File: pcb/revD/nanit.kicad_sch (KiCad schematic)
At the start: 73 parts, among them J1 USB_B_Micro, J2 AVR-ISP-6, P1 SSD1306 OLED 128x64 0.96", Q1 BC857, Q2 IRLML6344, Q4 BC847, SW1 Button 1, SW2 Button 2, U1 LTC4054ES5-4.2, U2 ATmega328P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

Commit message: revD
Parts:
- removed C20, C21, C22, C23: 1uF, Capacitor_SMD:C_0805_2012Metric_Pad1.18x1.45mm_HandSolder, symbol Device:C
- removed C24*1, C25: 4u7, Capacitor_SMD:C_0805_2012Metric_Pad1.18x1.45mm_HandSolder, symbol Device:C
- removed C26: 2u2, Capacitor_SMD:C_0805_2012Metric_Pad1.18x1.45mm_HandSolder, symbol Device:C
- removed C7: 100nF, Capacitor_SMD:C_0805_2012Metric_Pad1.15x1.40mm_HandSolder, symbol Device:C
- removed J2: AVR-ISP-6, Connector_PinHeader_2.54mm:PinHeader_2x03_P2.54mm_Vertical_SMD, symbol Connector:AVR-ISP-6
- removed JP1: SolderJumper_2_Open, Jumper:SolderJumper-2_P1.3mm_Open_TrianglePad1.0x1.5mm, symbol Jumper:SolderJumper_2_Open
- removed JP2: SolderJumper_2_Open, Jumper:SolderJumper-2_P1.3mm_Bridged_Pad1.0x1.5mm, symbol Jumper:SolderJumper_2_Bridged
- removed JP3: SolderJumper_3_Bridged12, Jumper:SolderJumper-3_P1.3mm_Bridged2Bar12_Pad1.0x1.5mm, symbol Jumper:SolderJumper_3_Bridged12
- removed P1: SSD1306 OLED 128x64 0.96", ribbon_connectors:SSD1306_ribbon, symbol oled_ribbon_connectors:SSD1306_ribbon
- removed R3*1: 4k7, Resistor_SMD:R_0805_2012Metric_Pad1.20x1.40mm_HandSolder, symbol Device:R
- removed R4*1: 390..910k, Resistor_SMD:R_0805_2012Metric_Pad1.20x1.40mm_HandSolder, symbol Device:R
- added D1: mR, LED_SMD:LED_0805_2012Metric_Pad1.15x1.40mm_HandSolder, symbol Device:LED
- added D10: Alarm, LED_SMD:LED_0805_2012Metric_Pad1.15x1.40mm_HandSolder, symbol Device:LED
- added D11: Time, LED_SMD:LED_0805_2012Metric_Pad1.15x1.40mm_HandSolder, symbol Device:LED
- added D2: SENSE, LED_SMD:LED_0805_2012Metric_Pad1.15x1.40mm_HandSolder, symbol Device:LED
- added D9: uR, LED_SMD:LED_0805_2012Metric_Pad1.15x1.40mm_HandSolder, symbol Device:LED
- added R3, R4: 10k, Resistor_SMD:R_0805_2012Metric_Pad1.20x1.40mm_HandSolder, symbol Device:R
- added TP1: RESET, TestPoint:TestPoint_Pad_1.5x1.5mm, symbol Connector:TestPoint_Flag
- added TP2: MISO, TestPoint:TestPoint_Pad_1.5x1.5mm, symbol Connector:TestPoint_Flag
- added TP3: MOSI, TestPoint:TestPoint_Pad_1.5x1.5mm, symbol Connector:TestPoint_Flag
- added TP4: SCK, TestPoint:TestPoint_Pad_1.5x1.5mm, symbol Connector:TestPoint_Flag
- added U4: HT16K33, Package_SO:SOIC-28W_7.5x17.9mm_P1.27mm, symbol eurocad:HT16K33
- added U5: 3461, footprints:7SEG-3461, symbol Display_Character:CC56-12SEKWA
- SW1, SW2: footprint Button_Switch_THT:SW_PUSH_6mm -> Button_Switch_SMD:SW_Push_1P1T_NO_6x6mm_H9.5mm
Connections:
- net GNDD: now also U4.1 (VSS)
- net VCC: now also R3.1, R4.1, U4.28 (VDD)
- net ~{RESET}: now also TP1.1
- net at U2.16 (PB4): now also TP2.1
- net SDA: now reaches U2.27 (PC4)
- net SDA: now also R3.2, U4.27 (SDA)
- net SCL: now reaches U2.28 (PC5)
- net SCL: now also R4.2, U4.26 (SCL)
- net LCD_VCC: no longer names the net of U2.23 (PC0)
- net OLED_CLK: no longer names the net of U2.17 (PB5)
- net OLED_CLK: now also TP4.1
- net OLED_CS: no longer names the net of U2.13 (PB1)
- net OLED_DC: no longer names the net of U2.14 (PB2)
- net OLED_MOSI: no longer names the net of U2.15 (PB3)
- net OLED_MOSI: now also TP3.1
- net OLED_RESET: no longer names the net of U2.24 (PC1)
- new net a: D2.2 (A), U4.25 (ROW0_A2), U5.11 (a)
- new net b: D9.2 (A), U4.24 (ROW1_A1), U5.7 (b)
- new net c: D1.2 (A), U4.23 (ROW2_A0), U5.4 (c)
- new net d: D10.2 (A), U4.22 (ROW3_K1), U5.2 (d)
- new net d1: U4.2 (COM0_AD), U5.12 (CC1)
- new net d2: U4.3 (COM1_KS0), U5.9 (CC2)
- new net d3: U4.5 (COM3_KS2), U5.8 (CC3)
- new net d4: U4.6 (COM4), U5.6 (CC4)
- new net dp: U4.18 (ROW7_K5), U5.3 (DPX)
- new net dx: D1.1 (K), D10.1 (K), D11.1 (K), D2.1 (K), D9.1 (K), U4.4 (COM2_KS1)
- new net e: D11.2 (A), U4.21 (ROW4_K2), U5.1 (e)
- new net f: U4.20 (ROW5_K3), U5.10 (f)
- new net g: U4.19 (ROW6_K4), U5.5 (g)
- no-connect marks 15 -> 26
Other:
- moved on the sheet: C12, C13, C14, C15, C16, C17, D5, D6, D7, D8, L1, Q2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

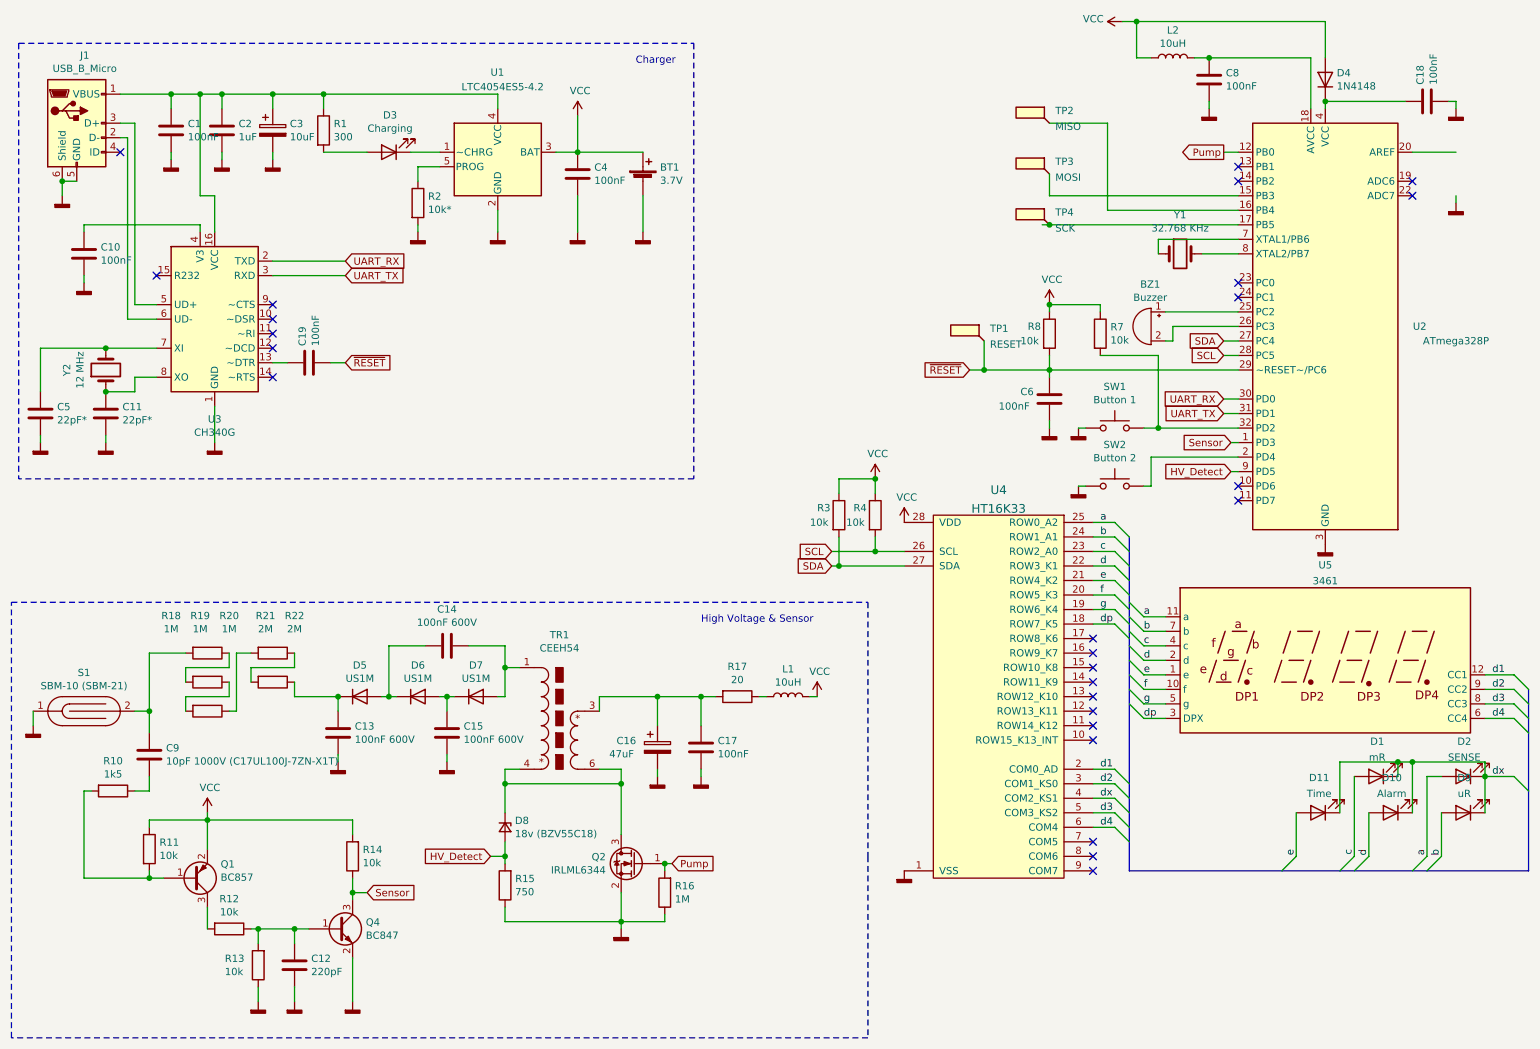
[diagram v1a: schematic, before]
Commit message: revD fixes - missing AREF capacitor C7
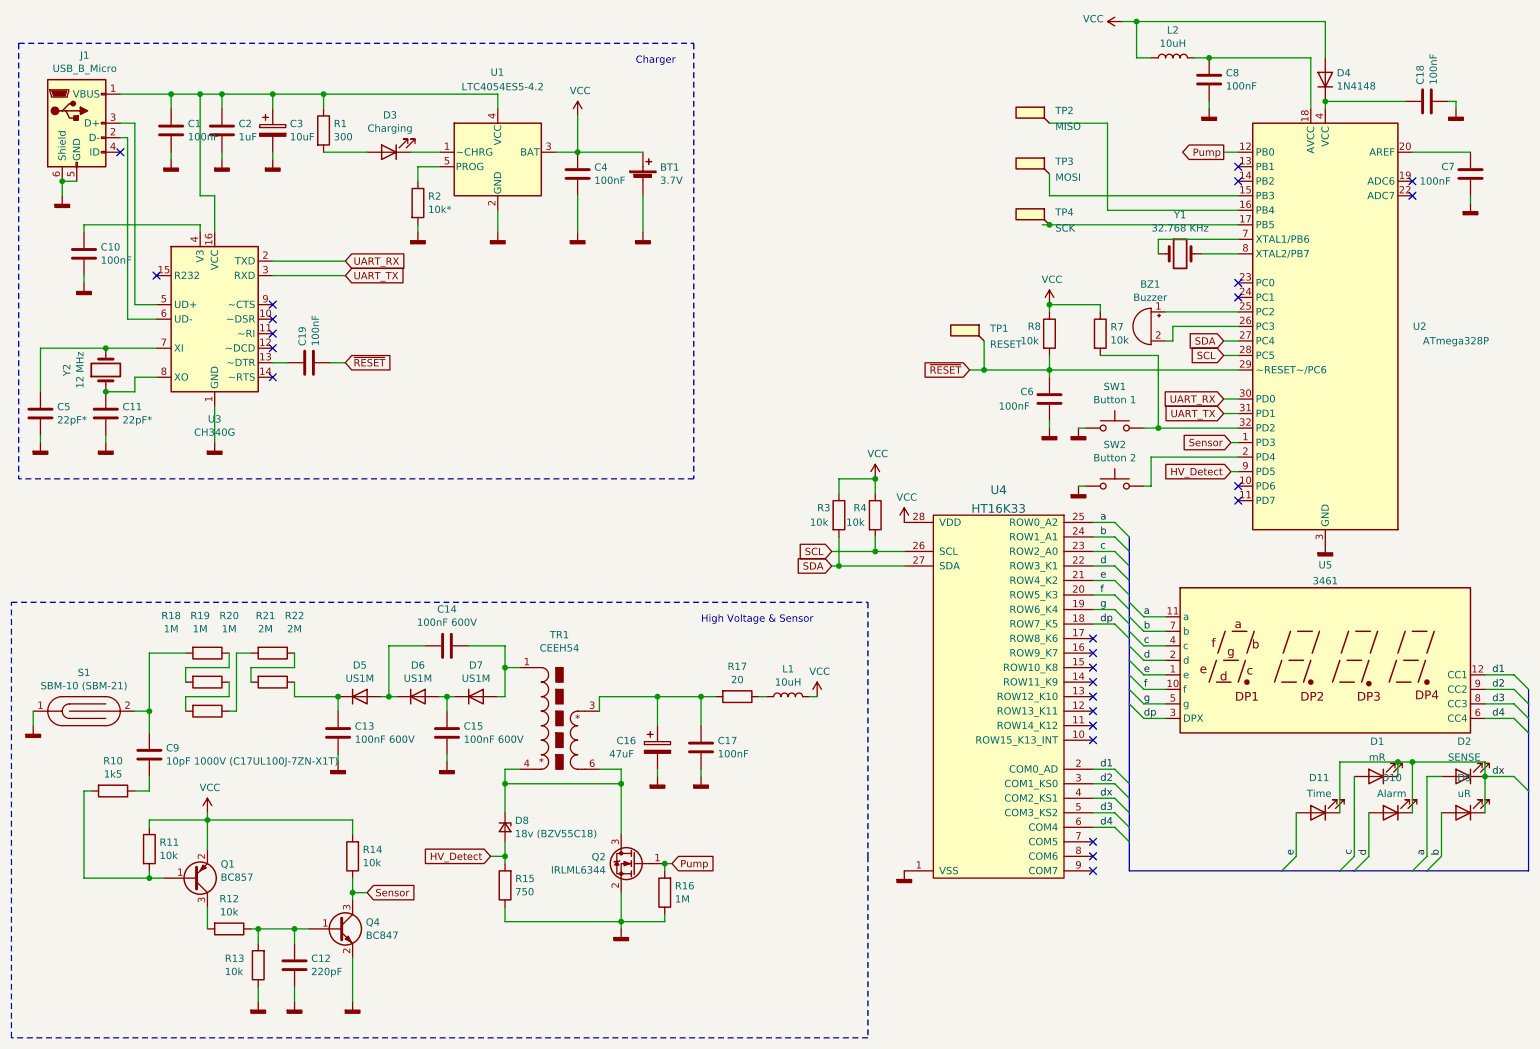
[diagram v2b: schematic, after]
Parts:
- added C7: 100nF, Capacitor_SMD:C_0805_2012Metric_Pad1.18x1.45mm_HandSolder, symbol Device:C
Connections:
- net GNDD: now also C7.2
- net at U2.20 (AREF): now also C7.1
